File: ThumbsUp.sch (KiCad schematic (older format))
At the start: 125 parts, among them J1 Conn_01x04_Male, J10 Raiser_Male, J11 Raiser_Female, J12 Raiser_Male, J13 Raiser_Female, J14 Raiser_Male, J15 Raiser_Female, J16 Raiser_Male, J17 Raiser_Female, J18 Raiser_Male, J19 52559-1233, J2 Conn_01x04_Male, J20 Conn_01x04_Female, J21 Conn_01x04_Female, J22 Conn_01x04_Female, J23 Conn_01x04_Female, J24 Conn_01x04_Male, J25 Conn_01x04_Male, J26 Conn_01x04_Male, J27 Conn_01x04_Male, J28 Conn_01x04_Female, J29 Conn_01x04_Female, J3 Conn_01x04_Female, J30 Conn_01x04_Female, J31 Conn_01x04_Female, J32 Battery, J4 Conn_01x04_Male, J5 Conn_01x04_Female, J6 Conn_01x04_Male, J7 Conn_01x04_Male, J8 Conn_01x04_Male, J9 Raiser_Female, SW1 SW_Push, SW2 SW_DIP_x01, U1 ProMicro

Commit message: v9 Added the third key to the thumbcluster.
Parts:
- added D45, D46: D_Small, Diode_SMD:D_SOD-123, symbol Device:D_Small
- added J33, J34: Conn_01x04_Female, Connector_PinSocket_2.54mm:PinSocket_1x04_P2.54mm_Vertical, symbol Connector:Conn_01x04_Female
- added J35, J36, J37: Raiser_Female, Connector_PinSocket_2.54mm:PinSocket_1x04_P2.54mm_Vertical, symbol Connector:Conn_01x04_Female
- added J38: 52559-1233, 52559-1233:525591233, symbol ThumbsUp-rescue:52559-1233-52559-1233
- added MX45: SwThL, keyswitches:Kailh_socket_PG1350_optional, symbol ThumbsUp-rescue:MX-NoLED-MX_Alps_Hybrid
- added MX46: SwThR, keyswitches:Kailh_socket_PG1350_optional, symbol ThumbsUp-rescue:MX-NoLED-MX_Alps_Hybrid
- added MX47: SwLMOD, keyswitches:Kailh_socket_PG1350_optional, symbol ThumbsUp-rescue:MX-NoLED-MX_Alps_Hybrid
- added MX48: SwLSHFT, keyswitches:Kailh_socket_PG1350_optional, symbol ThumbsUp-rescue:MX-NoLED-MX_Alps_Hybrid
- added MX49: SwRSHFT, keyswitches:Kailh_socket_PG1350_optional, symbol ThumbsUp-rescue:MX-NoLED-MX_Alps_Hybrid
- added MX50: SwRMOD, keyswitches:Kailh_socket_PG1350_optional, symbol ThumbsUp-rescue:MX-NoLED-MX_Alps_Hybrid
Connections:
- net COL1: now also J14.1 (Pin_1)
- net COLA: now also J14.4 (Pin_4)
- net ROW3: now also D45.1 (K), D46.1 (K)
- net at J14.2 (Pin_2): now also D45.2 (A)
- net at J14.3 (Pin_3): now also D46.2 (A)
- new net: J35.1 (Pin_1), MX45.1 (COL)
- new net: J35.2 (Pin_2), MX45.2 (ROW)
- new net: J35.4 (Pin_4), MX46.1 (COL)
- new net: J35.3 (Pin_3), MX46.2 (ROW)
- new net: J33.4 (Pin_4), MX48.1 (COL)
- new net: J33.3 (Pin_3), MX48.2 (ROW)
- new net: J33.1 (Pin_1), MX47.1 (COL)
- new net: J33.2 (Pin_2), MX47.2 (ROW)
- new net: J34.4 (Pin_4), MX50.1 (COL)
- new net: J34.3 (Pin_3), MX50.2 (ROW)
- new net: J34.1 (Pin_1), MX49.1 (COL)
- new net: J34.2 (Pin_2), MX49.2 (ROW)
- new net GND-TOP2: J37.4 (Pin_4), J38.11
- new net SCL-TOP2: J37.3 (Pin_3), J38.9
- new net SDA-TOP2: J37.2 (Pin_2), J38.10
- new net VCC-TOP2: J37.1 (Pin_1), J38.12
- no-connect marks 46 -> 59
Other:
- note added: "Three-key thumbcluster"
- note added: "Two-key thumbcluster"
- moved on the sheet: J13, J14

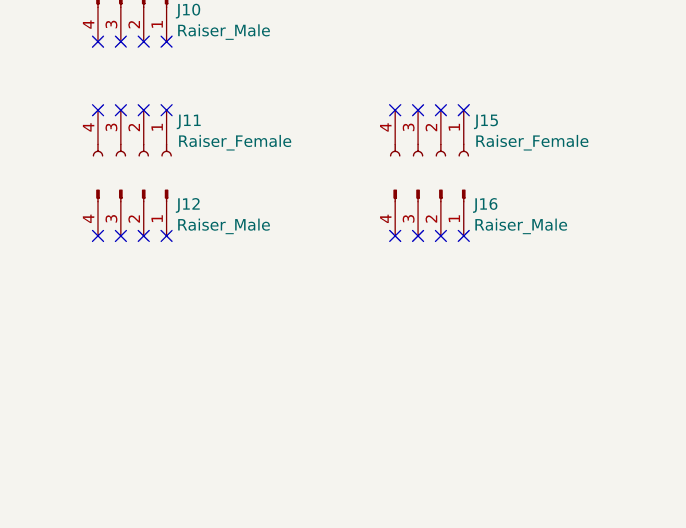
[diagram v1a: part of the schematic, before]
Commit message: v9 Redrew the lower PCB, added the silkscreens.
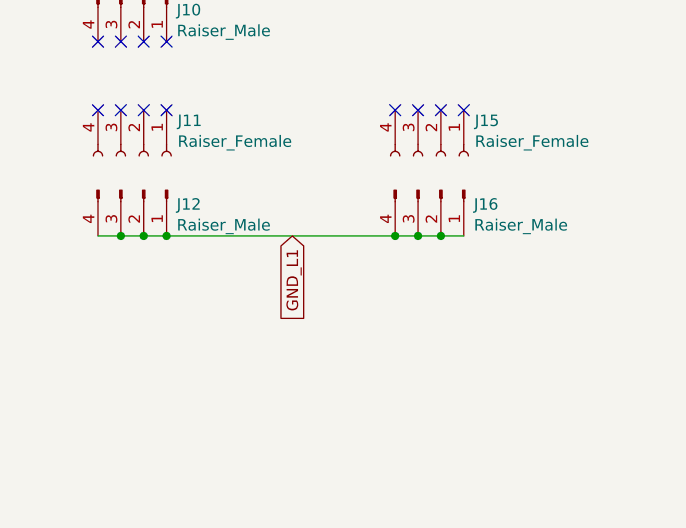
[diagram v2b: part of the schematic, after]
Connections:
- net GND_L1: now reaches J12.1 (Pin_1)
- net GND_L1: now also J12.2 (Pin_2), J12.3 (Pin_3), J12.4 (Pin_4), J16.1 (Pin_1), J16.2 (Pin_2), J16.3 (Pin_3), J16.4 (Pin_4)
- no-connect marks 59 -> 51
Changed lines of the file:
@@
-	0    1    1    0
-$EndComp
-$Comp
-L Connector:Conn_01x04_Male J12
-U 1 1 6206CD4F
-P 1750 12550
-F 0 "J12" V 1812 12694 50  0000 L CNN
-F 1 "Raiser_Male" V 1903 12694 50  0000 L CNN
-F 2 "Connector_PinHeader_2.54mm:PinHeader_1x04_P2.54mm_Vertical" H 1750 12550 50  0001 C CNN
-F 3 "~" H 1750 12550 50  0001 C CNN
-	1    1750 12550
 	0    1    1    0
 $EndComp
@@
 NoConn ~ 1750 12200
 NoConn ~ 1850 12200
-NoConn ~ 1550 12750
-NoConn ~ 1650 12750
-NoConn ~ 1750 12750
-NoConn ~ 1850 12750
 $Comp
 L Connector:Conn_01x04_Female J9
@@
 NoConn ~ 3050 12200
 NoConn ~ 3150 12200
-NoConn ~ 2850 12750
-NoConn ~ 2950 12750
-NoConn ~ 3050 12750
-NoConn ~ 3150 12750
 $Comp
 L Connector:Conn_01x04_Female J17
@@
 Text Notes 14400 2850 0    50   ~ 0
 Three-key thumbcluster
+$Comp
+L Connector:Conn_01x04_Male J12
+U 1 1 6206CD4F
+P 1750 12550
+F 0 "J12" V 1812 12694 50  0000 L CNN
+F 1 "Raiser_Male" V 1903 12694 50  0000 L CNN
+F 2 "Connector_PinHeader_2.54mm:PinHeader_1x04_P2.54mm_Vertical" H 1750 12550 50  0001 C CNN
+F 3 "~" H 1750 12550 50  0001 C CNN
+	1    1750 12550
+	0    1    1    0
+$EndComp
+Wire Wire Line
+	3150 12750 3050 12750
+Connection ~ 1650 12750
+Wire Wire Line
+	1650 12750 1550 12750
+Connection ~ 1750 12750
+Wire Wire Line
+	1750 12750 1650 12750
+Connection ~ 1850 12750
+Wire Wire Line
+	1850 12750 1750 12750
+Connection ~ 2850 12750
+Wire Wire Line
+	2850 12750 1850 12750
+Connection ~ 2950 12750
+Wire Wire Line
+	2950 12750 2850 12750
+Connection ~ 3050 12750
+Wire Wire Line
+	3050 12750 2950 12750
+Text GLabel 2400 12750 3    50   Input ~ 0
+GND_L1
 $EndSCHEMATC
